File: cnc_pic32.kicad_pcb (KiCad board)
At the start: 4 copper layers, 96 x 96 mm, 111 parts, among them J1 icd, J13 mrf24j40_tp, J14 mrf24j40_tp, J18 USB_B_Mini, J2 ST7789 oled 128x64, J20 pololu, J21 pololu, J22 pololu, J23 conector oled ST1306 128x32, J24 pololu, J25 pololu, J5 USB_B_Mini, Q1 2N7002, SW2 up, U1 PIC32MX795F512L-80x-PF, U2 FT232BM, U3 LM1117DT-3.3, U4 MRF24J40MA, U5 LM1117DT-3.3, Y2 6MHZ

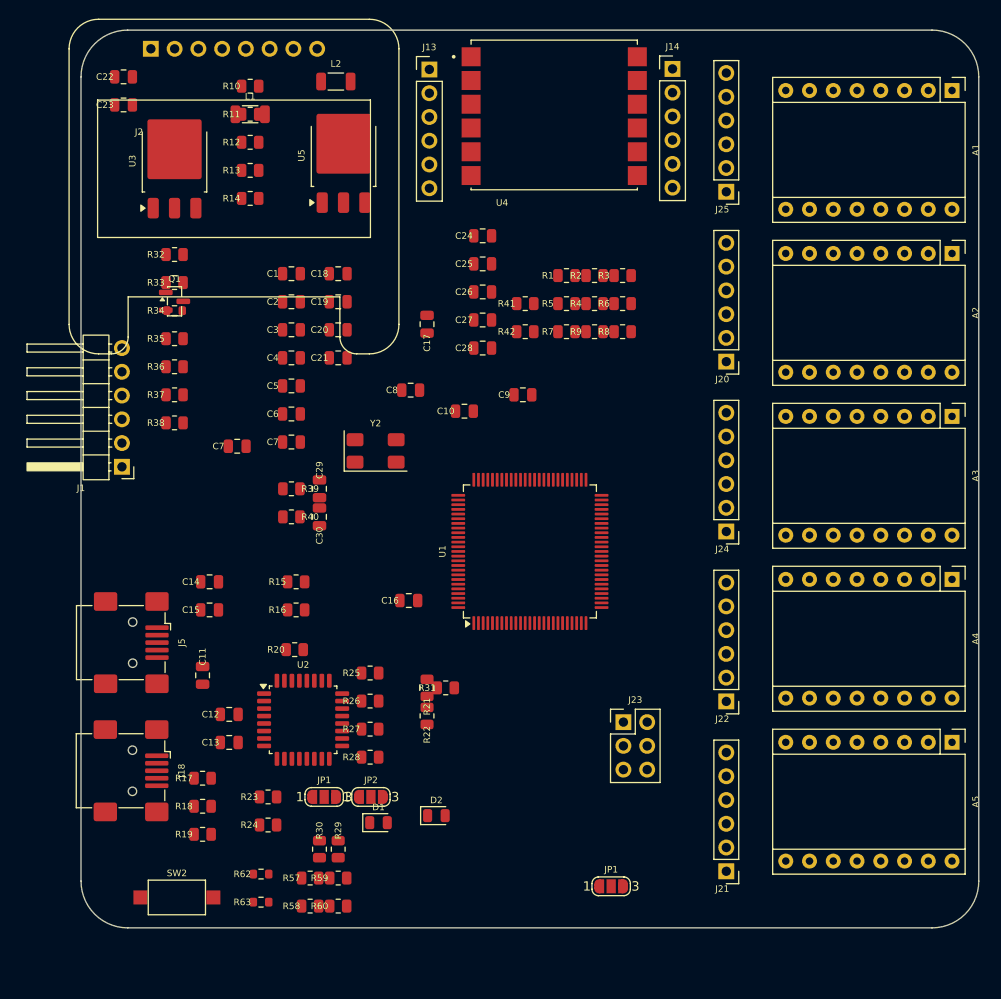
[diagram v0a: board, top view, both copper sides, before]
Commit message: feat: PCB layout updates, schematic changes, fp-lib-table config
- cnc_pic32.kicad_pcb: component repositioning, board outline, text formatting
- cnc_pic32.kicad_prl/pro: project settings updates
- fp-lib-table: add Library path to Library.pretty
- mcu.kicad_sch: PIC32 pin configuration updates
- zigbee.kicad_sch: MRF24J40 module updates
- oscilator.kicad_sch: crystal configuration
- power.kicad_sch/power_ft232.kicad_sch: power supply updates
- oled.kicad_sch: OLED display connections
- idc.kicad_sch: IDC connector updates
- osc_ft232.kicad_sch: FT232 crystal
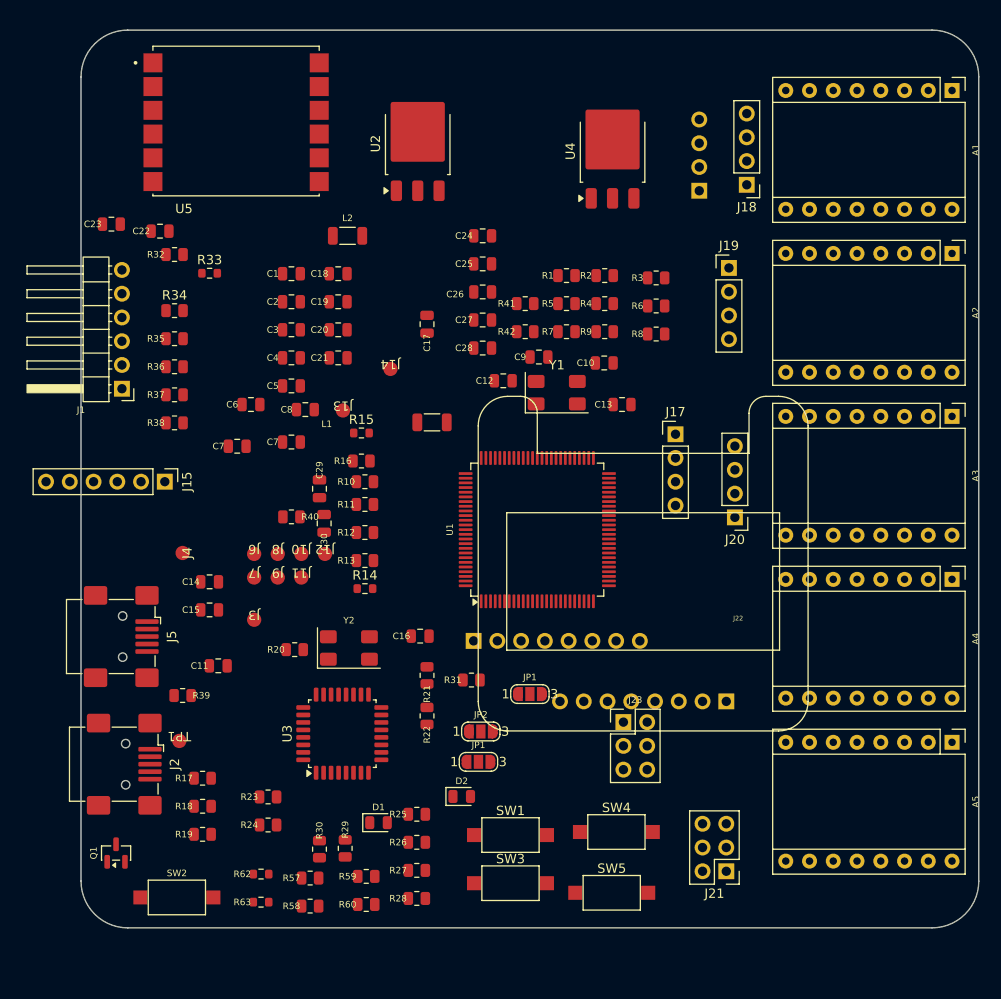
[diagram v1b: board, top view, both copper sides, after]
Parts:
- removed J25: pololu, kiC:PinHeader_1x06_P2.54mm_Vertical
- added J10: tp_ft232_, Library:connector_pin1, F.Cu at (75.6, 82.0)
- added J11: tp_ft232_, Library:connector_pin1, F.Cu at (75.6, 84.5)
- added J12: tp_ft232_, Library:connector_pin1, F.Cu at (78.1, 82.0)
- added J15: pololu, Library:PinHeader_1x06_P2.54mm_Vertical, F.Cu at (61.0, 74.3)
- added J16: pololu, Connector_PinHeader_2.54mm:PinHeader_1x04_P2.54mm_Vertical, B.Cu at (118.1, 43.2)
- added J17: pololu, Connector_PinHeader_2.54mm:PinHeader_1x04_P2.54mm_Vertical, F.Cu at (115.6, 69.2)
- added J19: pololu, Connector_PinHeader_2.54mm:PinHeader_1x04_P2.54mm_Vertical, F.Cu at (121.3, 51.4)
- added J3: tp_ft232_, Library:connector_pin1, F.Cu at (70.5, 89.1)
- added J4: tp_ft232_, Library:connector_pin1, F.Cu at (62.9, 81.9)
- added J6: tp_ft232_, Library:connector_pin1, F.Cu at (70.5, 82.0)
- added J7: tp_ft232_, Library:connector_pin1, F.Cu at (70.5, 84.5)
- added J8: tp_ft232_, Library:connector_pin1, F.Cu at (73.0, 82.0)
- added J9: tp_ft232_, Library:connector_pin1, F.Cu at (73.0, 84.5)
- added SW1: power, Button_Switch_SMD:SW_SPST_CK_RS282G05A3, F.Cu at (97.9, 112.1)
- added SW3: down, Button_Switch_SMD:SW_SPST_CK_RS282G05A3, F.Cu at (97.9, 117.2)
- added SW4: left, Button_Switch_SMD:SW_SPST_CK_RS282G05A3, F.Cu at (109.2, 111.8)
- added SW5: rigth, Button_Switch_SMD:SW_SPST_CK_RS282G05A3, F.Cu at (108.8, 118.2)
- added TP1: tp_pic+5, Library:connector_pin1, F.Cu at (62.5, 102.0)
- added Y1: 8MHZ, Crystal:Crystal_SMD_0603-4Pin_6.0x3.5mm, F.Cu at (102.9, 64.8)
- C10, C16, C9: value 15p -> 100nf
- C12, C13: value 33nf -> 15p
- C17: value 15p -> 33nf
- C18: value 100nf -> 33nf
- C21, C22: value 100nf -> 15p
- J13, J14: value mrf24j40_tp -> tp_ft232_; footprint Connector_PinHeader_2.54mm:PinHeader_1x06_P2.54mm_Vertical -> Library:connector_pin1
- J18: value USB_B_Mini -> pololu; footprint Connector_USB:USB_Mini-B_Wuerth_65100516121_Horizontal -> Connector_PinHeader_2.54mm:PinHeader_1x04_P2.54mm_Vertical
- J2: value ST7789 oled 128x64 -> USB_B_Mini; footprint kiC:Adafruit_SSD1306_No_Mounting_Holes_pads -> Library:USB_Mini-B_Wuerth_65100516121_Horizontal
- J20: footprint kiC:PinHeader_1x06_P2.54mm_Vertical -> Connector_PinHeader_2.54mm:PinHeader_1x04_P2.54mm_Vertical
- J21: value pololu -> conector oled ST1306 128x32; footprint kiC:PinHeader_1x06_P2.54mm_Vertical -> Connector_PinHeader_2.54mm:PinHeader_2x03_P2.54mm_Vertical
- J22: value pololu -> Adafruit ST7789; footprint kiC:PinHeader_1x06_P2.54mm_Vertical -> Library:Adafruit_SSD1306_No_Mounting_Holes_pads
- J24: value pololu -> Adafruit ST7789; footprint kiC:PinHeader_1x06_P2.54mm_Vertical -> Library:Adafruit_SSD1306_No_Mounting_Holes_pads; moved to B.Cu
- J5: footprint Connector_USB:USB_Mini-B_Wuerth_65100516121_Horizontal -> Library:USB_Mini-B_Wuerth_65100516121_Horizontal
- R1, R22: value 100 -> 10K
- R10, R13: value 10K -> 2k2
- R11, R12: value 0 -> 2k2
- R14: value 100 -> 2k2; footprint Resistor_SMD:R_0805_2012Metric -> Resistor_SMD:R_0603_1608Metric
- R15: value 1K -> 2k2; footprint Resistor_SMD:R_0805_2012Metric -> Resistor_SMD:R_0603_1608Metric
- R16: value 1M -> 10K
- R2: value 100 -> 0
- R20: value 10K -> 100
- R24: value 10K -> 1K5
- R27: value 1K5 -> 4K7
- R28: value 4K7 -> 27
- R3: value 10K -> 0
- R30: value 27 -> 10K
- R31: value 10K -> 1k
- R32, R38: value 2k2 -> 1k
- R33: footprint Resistor_SMD:R_0805_2012Metric -> Resistor_SMD:R_0603_1608Metric
- R34: footprint Resistor_SMD:R_0603_1608Metric -> Resistor_SMD:R_0805_2012Metric
- R39: value 22 -> 1k
- R4: value 22 -> 10K
- R5: value 1k -> 100
- R6: value 22 -> 1K
- R7: value 100 -> 1M
- R8: value 100 -> 22
- R9: value 1k -> 22
- U2: value FT232BM -> LM1117DT-3.3; footprint Package_QFP:LQFP-32_7x7mm_P0.8mm -> Package_TO_SOT_SMD:TO-252-3_TabPin2
- U3: value LM1117DT-3.3 -> FT232BM; footprint Package_TO_SOT_SMD:TO-252-3_TabPin2 -> Package_QFP:LQFP-32_7x7mm_P0.8mm
- U4: value MRF24J40MA -> LM1117DT-3.3; footprint Library:MODULE_MRF24J40MA -> Package_TO_SOT_SMD:TO-252-3_TabPin2
- U5: value LM1117DT-3.3 -> MRF24J40MA; footprint Package_TO_SOT_SMD:TO-252-3_TabPin2 -> Library:MODULE_MRF24J40MA
- moved J18 90.8 mm to (123.2, 42.5), turned to 180 degrees
- moved J2 76.5 mm to (56.8, 104.5), turned to -90 degrees
- moved U3 63.8 mm to (79.9, 101.2)
- moved U2 62.8 mm to (88.0, 38.1), turned to 90 degrees
- moved Q1 59.3 mm to (55.8, 114.0), turned to 90 degrees
- moved C13 55.4 mm to (109.9, 66.0)
- moved C12 46.2 mm to (97.2, 63.5)
- moved R10 44.0 mm to (82.4, 74.3)
- moved J14 44.0 mm to (85.1, 62.2)
- moved R11 43.5 mm to (82.4, 76.7)
- moved R12 43.5 mm to (82.4, 79.7)
- moved R13 43.5 mm to (82.4, 82.7)
- moved R14 43.5 mm to (82.4, 85.7)
- moved L1 38.3 mm to (89.5, 67.9)
- moved J13 37.6 mm to (80.0, 66.7)
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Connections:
- A1 pad 13: unconnected-(A1-~{RESET}-Pad13) -> /MCU/RA0
- A1 pad 14: unconnected-(A1-~{SLEEP}-Pad14) -> /MCU/RA1
- A1 pad 15: unconnected-(A1-STEP-Pad15) -> /MCU/RA3
- A1 pad 16: unconnected-(A1-DIR-Pad16) -> /MCU/RA4
- A1 pad 9: unconnected-(A1-~{ENABLE}-Pad9) -> /MCU/RA2
- A2 pad 13: unconnected-(A2-~{RESET}-Pad13) -> /MCU/RA5
- A2 pad 14: unconnected-(A2-~{SLEEP}-Pad14) -> /MCU/RA6
- A2 pad 15: unconnected-(A2-STEP-Pad15) -> /MCU/RA9
- A2 pad 16: unconnected-(A2-DIR-Pad16) -> /MCU/RA10
- A2 pad 9: unconnected-(A2-~{ENABLE}-Pad9) -> /MCU/RA7
- A3 pad 13: unconnected-(A3-~{RESET}-Pad13) -> /MCU/RB0
- A3 pad 14: unconnected-(A3-~{SLEEP}-Pad14) -> /MCU/RB1
- A3 pad 15: unconnected-(A3-STEP-Pad15) -> /MCU/RB3
- A3 pad 16: unconnected-(A3-DIR-Pad16) -> /MCU/RB4
- A3 pad 9: unconnected-(A3-~{ENABLE}-Pad9) -> /MCU/RB2
- A4 pad 13: unconnected-(A4-~{RESET}-Pad13) -> /MCU/RE9
- A4 pad 14: unconnected-(A4-~{SLEEP}-Pad14) -> /MCU/RE8
- A4 pad 15: unconnected-(A4-STEP-Pad15) -> /MCU/RE6
- A4 pad 9: unconnected-(A4-~{ENABLE}-Pad9) -> /MCU/RE7
- A5 pad 13: unconnected-(A5-~{RESET}-Pad13) -> /MCU/RE4
- A5 pad 14: unconnected-(A5-~{SLEEP}-Pad14) -> /MCU/RE3
- A5 pad 15: unconnected-(A5-STEP-Pad15) -> /MCU/RE1
- A5 pad 16: unconnected-(A5-DIR-Pad16) -> /MCU/RE0
- A5 pad 9: unconnected-(A5-~{ENABLE}-Pad9) -> /MCU/RE2
- C10 pad 1: /oscilator/OSC1 -> +3.3V
- C11 pad 1: /Ft232/mclr -> +3.3V
- C11 pad 2: /Ft232/FT_CTS -> GND
- C12 pad 1: Net-(U2-AVCC) -> Net-(C12-Pad1)
- C13 pad 1: Net-(J3-Pin_1) -> /MCU/OSC2
- C14 pad 2: /Ft232/V+_USB -> Net-(TP1-Pin_1)
- C16 pad 1: /Ft232/FT_XTIN -> /Ft232/mclr
- C16 pad 2: GND -> /Ft232/FT_CTS
- C17 pad 1: /Ft232/FT_XTOUT -> Net-(U3-AVCC)
- C18 pad 1: +3V3 -> Net-(J3-Pin_1)
- C19 pad 1: +3V3 -> GND
- C19 pad 2: GND -> /Ft232/V+_USB
- C21 pad 1: GND -> /Ft232/FT_XTIN
- C21 pad 2: +3V3 -> GND
- C22 pad 1: +3.3V -> /Ft232/FT_XTOUT
- C23 pad 1: +3.3V -> +3V3
- C24 pad 1: +3.3V -> +3V3
- C25 pad 1: +3.3V -> GND
- C25 pad 2: GND -> +3V3
- C26 pad 1: +3.3V -> GND
- C26 pad 2: GND -> +3V3
- C6 pad 1: unconnected-(C6-Pad1) -> +3.3V
- C6 pad 2: unconnected-(C6-Pad2) -> GND
- C7 pad 1: unconnected-(C7-Pad1) -> +3.3V
- C7 pad 2: unconnected-(C7-Pad2) -> GND
- C9 pad 1: Net-(C9-Pad1) -> +3.3V
- J13 pad 1: GND -> /Ft232/tp_ft232/FT_DTR
- J14 pad 1: GND -> /Ft232/tp_ft232/+5v
- J18 pad 1: Net-(J18-VBUS) -> Net-(A3-2B)
- J18 pad 2: Net-(J18-D-) -> Net-(A3-2A)
- J18 pad 3: Net-(J18-D+) -> Net-(A3-1A)
- J18 pad 4: unconnected-(J18-ID-Pad4) -> Net-(A3-1B)
- J2 pad 1: GND -> Net-(J2-VBUS)
- J2 pad 2: +3.3V -> Net-(J2-D-)
- J2 pad 3: /Oled/sda -> Net-(J2-D+)
- J2 pad 4: /Oled/scl -> unconnected-(J2-ID-Pad4)
- J2 pad 5: unconnected-(J2-Pin_5-Pad5) -> GND
- J2 pad 6: unconnected-(J2-Pin_6-Pad6) -> GND
- J20 pad 1: Net-(A2-2B) -> Net-(A5-2B)
- J20 pad 2: Net-(A2-2A) -> Net-(A5-2A)
- J20 pad 3: Net-(A2-1A) -> Net-(A5-1A)
- J20 pad 4: Net-(A2-1B) -> Net-(A5-1B)
- J21 pad 1: Net-(A5-2B) -> GND
- J21 pad 2: Net-(A5-2A) -> +3.3V
- J21 pad 3: Net-(A5-1A) -> /MCU/scl
- J21 pad 4: Net-(A5-1B) -> /MCU/sda
- J21 pad 5: (no net) -> unconnected-(J21-Pin_5-Pad5)
- J21 pad 6: (no net) -> unconnected-(J21-Pin_6-Pad6)
- J22 pad 1: Net-(A4-2B) -> GND
- J22 pad 2: Net-(A4-2A) -> +3.3V
- J22 pad 3: Net-(A4-1A) -> /MCU/sda
- J22 pad 4: Net-(A4-1B) -> /MCU/scl
- J22 pad 5: (no net) -> unconnected-(J22-Pin_5-Pad5)
- J22 pad 6: (no net) -> unconnected-(J22-Pin_6-Pad6)
- J23 pad 3: /Oled/scl -> /MCU/scl
- J23 pad 4: /Oled/sda -> /MCU/sda
- J24 pad 1: Net-(A3-2B) -> GND
- J24 pad 2: Net-(A3-2A) -> +3.3V
- J24 pad 3: Net-(A3-1A) -> /MCU/sda
- J24 pad 4: Net-(A3-1B) -> /MCU/scl
- J24 pad 5: (no net) -> unconnected-(J24-Pin_5-Pad5)
- J24 pad 6: (no net) -> unconnected-(J24-Pin_6-Pad6)
- JP1 pad 1: TXD -> RXD
- JP1 pad 2: /Ft232/TX_MCU -> /Ft232/RX_MCU
- JP1 pad 3: TX_Rpi -> RX_Rpi
- JP2 pad 1: RXD -> TXD
- JP2 pad 2: /Ft232/RX_MCU -> /Ft232/TX_MCU
- JP2 pad 3: RX_Rpi -> TX_Rpi
- L1 pad 1: Net-(J4-Pin_1) -> Net-(J2-VBUS)
- L1 pad 2: /Ft232/V+_USB -> Net-(TP1-Pin_1)
- L2 pad 1: Net-(J18-VBUS) -> Net-(J4-Pin_1)
- L2 pad 2: Net-(TP17-Pin_1) -> /Ft232/V+_USB
- R1 pad 1: unconnected-(R1-Pad1) -> +3.3V
- R1 pad 2: unconnected-(R1-Pad2) -> /Ft232/mclr
- R10 pad 2: /Ft232/mclr -> /MCU/RD5
- R11 pad 1: /MCU/RD0 -> +3.3V
- R11 pad 2: /MCU/scl -> /MCU/RD4
- R12 pad 1: /MCU/RD1 -> +12V
- R12 pad 2: /MCU/sda -> Net-(R12-Pad2)
- R13 pad 1: unconnected-(R13-Pad1) -> SW_PWR
- R13 pad 2: unconnected-(R13-Pad2) -> GND
- R14 pad 1: unconnected-(R14-Pad1) -> +3.3V
- R14 pad 2: unconnected-(R14-Pad2) -> /MCU/RD7
- R15 pad 1: /oscilator/OSC0 -> +3.3V
- R15 pad 2: Net-(C9-Pad1) -> /MCU/RD6
- R16 pad 1: Net-(C9-Pad1) -> Net-(Q1-D)
- R16 pad 2: /oscilator/OSC1 -> /Ft232/V+_USB
- R17 pad 1: Net-(Q1-D) -> GND
- R17 pad 2: /Ft232/V+_USB -> /Ft232/FT
- R18 pad 1: GND -> /Ft232/FT_PWR_EN
- R18 pad 2: /Ft232/FT -> Net-(Q1-G)
- R19 pad 1: /Ft232/FT_PWR_EN -> +3V3
- R19 pad 2: Net-(Q1-G) -> Net-(D1-A)
- R2 pad 1: unconnected-(R2-Pad1) -> /MCU/RD1
- R2 pad 2: unconnected-(R2-Pad2) -> /MCU/sda
- R20 pad 1: +3V3 -> Net-(U3-D0/TXD)
- R20 pad 2: Net-(D1-A) -> /Ft232/RX_MCU
- R21 pad 1: Net-(U2-D0/TXD) -> Net-(U3-D1/RXD)
- R21 pad 2: /Ft232/RX_MCU -> /Ft232/TX_MCU
- R22 pad 1: Net-(U2-D1/RXD) -> +3V3
- R22 pad 2: /Ft232/TX_MCU -> Net-(D2-A)
- R23 pad 2: Net-(D2-A) -> Net-(U3-~{SLEEP})
- R24 pad 1: +3V3 -> Net-(U3-AVCC)
- R24 pad 2: Net-(U2-~{SLEEP}) -> /Ft232/V+_USB
- R25 pad 1: Net-(U2-AVCC) -> /Ft232/FT_RST_OUT
- R25 pad 2: /Ft232/V+_USB -> /Ft232/FT_USB_DP
- R27 pad 1: /Ft232/FT_RST_OUT -> /Ft232/V+_USB
- R27 pad 2: /Ft232/FT_USB_DP -> /Ft232/FT_RESET
- R28 pad 1: /Ft232/V+_USB -> /Ft232/FT_USB_BM
- R28 pad 2: /Ft232/FT_RESET -> Net-(J5-D+)
- R29 pad 1: /Ft232/FT_USB_BM -> /Ft232/FT_USB_DP
- R29 pad 2: Net-(J5-D+) -> Net-(J5-D-)
- R3 pad 1: unconnected-(R3-Pad1) -> /MCU/RD0
- R3 pad 2: unconnected-(R3-Pad2) -> /MCU/scl
- R30 pad 1: /Ft232/FT_USB_DP -> +3V3
- R30 pad 2: Net-(J5-D-) -> /Ft232/FT_RESET
- R31 pad 1: +3V3 -> +3.3V
- R31 pad 2: /Ft232/power_ft232/FT_RESET -> /MCU/scl
- R32 pad 2: /zigbee/RESET_mrf -> /MCU/sda
- R33 pad 1: +3.3V -> /MCU/RA6
- R33 pad 2: /zigbee/int -> GND
- R34 pad 1: /zigbee/WAKE_mrf -> /MCU/RA2
- R34 pad 2: GND -> +3.3V
- R35 pad 1: /zigbee/MISO_spi4 -> /MCU/RA0
- R36 pad 1: /zigbee/CS_spi4 -> +3.3V
- R36 pad 2: +3.3V -> /MCU/RA5
- R37 pad 2: /zigbee/SCK_spi4 -> /MCU/RA3
- R38 pad 2: /zigbee/MOSI_spi4 -> /MCU/scl
- R39 pad 1: /Usb_pic32/D+ -> +3.3V
- R39 pad 2: Net-(J18-D+) -> /MCU/sda
- R40 pad 1: /Usb_pic32/D- -> /MCU/D-
- R40 pad 2: Net-(J18-D-) -> Net-(J4-D-)
- R41 pad 2: /Oled/sda -> /MCU/sda
- R42 pad 2: /Oled/scl -> /MCU/scl
- R6 pad 1: unconnected-(R6-Pad1) -> /MCU/OSC1
- R6 pad 2: unconnected-(R6-Pad2) -> Net-(C12-Pad1)
- R7 pad 1: unconnected-(R7-Pad1) -> Net-(C12-Pad1)
- R7 pad 2: unconnected-(R7-Pad2) -> /MCU/OSC2
- R8 pad 1: unconnected-(R8-Pad1) -> /MCU/D+
- R8 pad 2: unconnected-(R8-Pad2) -> Net-(J2-D+)
- R9 pad 1: unconnected-(R9-Pad1) -> /MCU/D-
- R9 pad 2: unconnected-(R9-Pad2) -> Net-(J2-D-)
- U1 pad 87: /MCU/RF0 -> /Ft232/RX_MCU
- U1 pad 88: /MCU/RF1 -> /Ft232/TX_MCU
- U2 pad 1: /Ft232/FT_EESK -> GND
- U2 pad 2: /Ft232/FT_EEDATA -> +3V3
- U2 pad 3: /Ft232/V+_USB -> Net-(TP1-Pin_1)
- U3 pad 1: GND -> /Ft232/FT_EESK
- U3 pad 2: +3V3 -> /Ft232/FT_EEDATA
- U4 pad 2: /zigbee/RESET_mrf -> +3V3
- U4 pad 3: /zigbee/WAKE_mrf -> /Ft232/V+_USB
- U5 pad 2: +3V3 -> /MCU/RA4
- U5 pad 3: Net-(TP17-Pin_1) -> /MCU/RA6

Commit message: fix: remove orphaned duplicate footprints C7 and JP1 from PCB
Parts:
- removed the C7 at (68.7, 70.5)
- removed the JP1 at (100.0, 97.0)
- moved J15 6.63 mm to (67.3, 76.2)
- moved J23 5.47 mm to (109.2, 105.4), turned to 90 degrees
- renumbered C18 to C31

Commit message: feat: PCB and project updates from KiCad
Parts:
- added C18: 33nf, Capacitor_SMD:C_0805_2012Metric, F.Cu at (99.5, 34.7)
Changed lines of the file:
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@@
 				)
 			)
-			(render_cache "C18" 0
+			(render_cache "C31" 0
 				(polygon
 					(pts
@@
 				(polygon
 					(pts
-						(xy 77.674047 52.3405) (xy 77.587964 52.3405) (xy 77.587964 51.790575) (xy 77.55371 51.819074)
-						(xy 77.506454 51.850029) (xy 77.456723 51.876938) (xy 77.41584 51.89461) (xy 77.41584 51.811176)
-						(xy 77.462669 51.786471) (xy 77.504614 51.75898) (xy 77.542059 51.728726) (xy 77.57641 51.694739)
-						(xy 77.601401 51.663542) (xy 77.618568 51.634735) (xy 77.674047 51.634735)
+						(xy 77.350316 52.154484) (xy 77.436399 52.143542) (xy 77.449783 52.19063) (xy 77.466811 52.224568)
+						(xy 77.486835 52.248261) (xy 77.512159 52.265984) (xy 77.54077 52.276641) (xy 77.573645 52.280318)
+						(xy 77.612359 52.275546) (xy 77.646127 52.261626) (xy 77.676184 52.238174) (xy 77.699388 52.207894)
+						(xy 77.713251 52.173505) (xy 77.718029 52.133711) (xy 77.713551 52.095716) (xy 77.70067 52.063505)
+						(xy 77.679305 52.035745) (xy 77.651445 52.014492) (xy 77.619066 52.001658) (xy 77.580826 51.997192)
+						(xy 77.555159 51.99932) (xy 77.520089 52.006766) (xy 77.52962 51.930172) (xy 77.543512 51.931155)
+						(xy 77.579336 51.927917) (xy 77.612115 51.918421) (xy 77.642503 51.902645) (xy 77.661596 51.886605)
+						(xy 77.675114 51.867123) (xy 77.683505 51.843522) (xy 77.686485 51.814681) (xy 77.682811 51.784673)
+						(xy 77.672187 51.759048) (xy 77.654429 51.736762) (xy 77.63144 51.719826) (xy 77.604267 51.709487)
+						(xy 77.571722 51.705859) (xy 77.539491 51.709499) (xy 77.511946 51.71998) (xy 77.488032 51.737317)
+						(xy 77.469271 51.760333) (xy 77.454749 51.79113) (xy 77.44499 51.831693) (xy 77.35895 51.81528)
+						(xy 77.369884 51.77313) (xy 77.385584 51.737459) (xy 77.405814 51.707317) (xy 77.430672 51.682009)
+						(xy 77.459831 51.661621) (xy 77.492308 51.646942) (xy 77.528715 51.637882) (xy 77.569841 51.634735)
+						(xy 77.607483 51.637528) (xy 77.642543 51.645738) (xy 77.675501 51.659312) (xy 77.70565 51.678045)
+						(xy 77.730055 51.70033) (xy 77.74936 51.726375) (xy 77.763684 51.75552) (xy 77.772138 51.785429)
+						(xy 77.774962 51.816562) (xy 77.772217 51.846067) (xy 77.764115 51.873419) (xy 77.750556 51.89914)
+						(xy 77.732249 51.921696) (xy 77.708473 51.941395) (xy 77.678364 51.958296) (xy 77.717553 51.971727)
+						(xy 77.749333 51.991585) (xy 77.77492 52.018007) (xy 77.793654 52.049813) (xy 77.805276 52.087147)
+						(xy 77.80937 52.13136) (xy 77.80511 52.176028) (xy 77.792663 52.216357) (xy 77.772006 52.253283)
+						(xy 77.742435 52.287456) (xy 77.707136 52.315207) (xy 77.667734 52.335029) (xy 77.623427 52.347212)
+						(xy 77.573132 52.351442) (xy 77.527643 52.347799) (xy 77.487517 52.337315) (xy 77.451825 52.320304)
+						(xy 77.419858 52.296603) (xy 77.392758 52.267291) (xy 77.372297 52.234266) (xy 77.358117 52.196943)
 					)
 				)
 				(polygon
 					(pts
-						(xy 78.168198 51.638352) (xy 78.207257 51.64865) (xy 78.241085 51.665175) (xy 78.270519 51.687993)
-						(xy 78.295256 51.716435) (xy 78.31252 51.747131) (xy 78.322914 51.780618) (xy 78.326469 51.817673)
-						(xy 78.323511 51.849334) (xy 78.314945 51.877358) (xy 78.300866 51.902474) (xy 78.281696 51.923934)
-						(xy 78.256212 51.942488) (xy 78.223203 51.958082) (xy 78.263914 51.975649) (xy 78.296242 51.998344)
-						(xy 78.321468 52.026214) (xy 78.339955 52.058998) (xy 78.351265 52.096064) (xy 78.355192 52.138456)
-						(xy 78.351105 52.18233) (xy 78.33921 52.221645) (xy 78.319567 52.257339) (xy 78.291591 52.290063)
-						(xy 78.258074 52.316418) (xy 78.219686 52.335454) (xy 78.175494 52.347291) (xy 78.124254 52.351442)
-						(xy 78.073007 52.347275) (xy 78.028806 52.335394) (xy 77.990406 52.31628) (xy 77.956874 52.289807)
-						(xy 77.928989 52.256997) (xy 77.909336 52.220944) (xy 77.89739 52.180958) (xy 77.893325 52.136618)
-						(xy 77.981708 52.136618) (xy 77.986018 52.172702) (xy 77.999147 52.207998) (xy 78.012693 52.229278)
-						(xy 78.029867 52.24698) (xy 78.051036 52.261426) (xy 78.086747 52.275584) (xy 78.125152 52.280318)
-						(xy 78.164631 52.275717) (xy 78.198127 52.262486) (xy 78.227007 52.240568) (xy 78.249183 52.211927)
-						(xy 78.262542 52.178705) (xy 78.267185 52.139524) (xy 78.262421 52.099744) (xy 78.248681 52.065884)
-						(xy 78.22581 52.036558) (xy 78.196138 52.014041) (xy 78.162075 52.00051) (xy 78.122288 51.995824)
-						(xy 78.083477 52.000457) (xy 78.050369 52.013826) (xy 78.021629 52.036087) (xy 77.999539 52.064978)
-						(xy 77.98629 52.098059) (xy 77.981708 52.136618) (xy 77.893325 52.136618) (xy 77.893274 52.136062)
-						(xy 77.897381 52.091475) (xy 77.909068 52.053615) (xy 77.927938 52.02117) (xy 77.95376 51.994044)
-						(xy 77.986247 51.973042) (xy 78.026673 51.958082) (xy 77.992711 51.942407) (xy 77.966694 51.923759)
-						(xy 77.9473 51.902218) (xy 77.933162 51.876897) (xy 77.924496 51.848189) (xy 77.921484 51.81528)
-						(xy 77.921756 51.812416) (xy 78.009448 51.812416) (xy 78.013169 51.844066) (xy 78.023834 51.87065)
-						(xy 78.041462 51.893327) (xy 78.064521 51.910519) (xy 78.091854 51.921015) (xy 78.124682 51.9247)
-						(xy 78.156574 51.921065) (xy 78.183378 51.910665) (xy 78.206234 51.893541) (xy 78.223949 51.87113)
-						(xy 78.234441 51.845992) (xy 78.238035 51.817203) (xy 78.234316 51.787176) (xy 78.223485 51.761103)
-						(xy 78.205251 51.738001) (xy 78.181766 51.720214) (xy 78.154938 51.709546) (xy 78.123741 51.705859)
-						(xy 78.092188 51.709491) (xy 78.065286 51.719948) (xy 78.041975 51.737275) (xy 78.023738 51.75984)
-						(xy 78.013066 51.784601) (xy 78.009448 51.812416) (xy 77.921756 51.812416) (xy 77.925003 51.778162)
-						(xy 77.935259 51.744868) (xy 77.952226 51.714598) (xy 77.976451 51.686796) (xy 78.005361 51.66455)
-						(xy 78.038773 51.64839) (xy 78.077543 51.638291) (xy 78.122801 51.634735)
+						(xy 78.218416 52.3405) (xy 78.132332 52.3405) (xy 78.132332 51.790575) (xy 78.098078 51.819074)
+						(xy 78.050822 51.850029) (xy 78.001091 51.876938) (xy 77.960208 51.89461) (xy 77.960208 51.811176)
+						(xy 78.007038 51.786471) (xy 78.048982 51.75898) (xy 78.086427 51.728726) (xy 78.120779 51.694739)
+						(xy 78.145769 51.663542) (xy 78.162936 51.634735) (xy 78.218416 51.634735)
 					)
 				)
@@
 			(offset
 				(xyz 0 0 0)
+			)
+			(scale
+				(xyz 1 1 1)
+			)
+			(rotate
+				(xyz 0 0 0)
+			)
+		)
+	)
+	(footprint "Capacitor_SMD:C_0805_2012Metric"
+		(layer "F.Cu")
+		(at 99.515 34.66)
+		(descr "Capacitor SMD 0805 (2012 Metric), square (rectangular) end terminal, IPC-7351 nominal, (Body size source: IPC-SM-782 page 76, https://www.pcb-3d.com/wordpress/wp-content/uploads/ipc-sm-782a_amendment_1_and_2.pdf, https://docs.google.com/spreadsheets/d/1BsfQQcO9C6DZCsRaXUlFlo91Tg2WpOkGARC1WS5S8t0/edit?usp=sharing)")
+		(tags "capacitor")
+		(property "Reference" "C18"
+			(at 0 -1.68 0)
+			(layer "F.SilkS")
+			(effects
+				(font
+					(size 1 1)
+					(thickness 0.15)
+				)
+			)
+		)
+		(property "Value" "33nf"
+			(at 0 1.68 0)
+			(layer "F.Fab")
+			(effects
+				(font
+					(size 1 1)
+					(thickness 0.15)
+				)
+			)
+		)
+		(property "Datasheet" ""
+			(at 0 0 0)
+			(layer "F.Fab")
+			(hide yes)
+			(effects
+				(font
+					(size 1.27 1.27)
+				)
+			)
+		)
+		(property "Description" ""
+			(at 0 0 0)
+			(layer "F.Fab")
+			(hide yes)
+			(effects
+				(font
+					(size 1.27 1.27)
+				)
+			)
+		)
+		(property ki_fp_filters "C_*")
+		(sheetname "/Ft232/")
+		(sheetfile "ft232.kicad_sch")
+		(units
+			(unit
+				(name "A")
+				(pins "1" "2")
+			)
+		)
+		(attr smd)
+		(duplicate_pad_numbers_are_jumpers no)
+		(fp_line
+			(start -0.261252 -0.735)
+			(end 0.261252 -0.735)
+			(stroke
+				(width 0.12)
+				(type solid)
+			)
+			(layer "F.SilkS")
+		)
+		(fp_line
+			(start -0.261252 0.735)
+			(end 0.261252 0.735)
+			(stroke
+				(width 0.12)
+				(type solid)
+			)
+			(layer "F.SilkS")
+		)
+		(fp_rect
+			(start -1.7 -0.98)
+			(end 1.7 0.98)
+			(stroke
+				(width 0.05)
+				(type solid)
+			)
+			(fill no)
+			(layer "F.CrtYd")
+		)
+		(fp_rect
+			(start -1 -0.625)
+			(end 1 0.625)
+			(stroke
+				(width 0.1)
+				(type solid)
+			)
+			(fill no)
+			(layer "F.Fab")
+		)
+		(fp_text user "${REFERENCE}"
+			(at 0 0 0)
+			(layer "F.Fab")
+			(effects
+				(font
+					(size 0.5 0.5)
+					(thickness 0.08)
+				)
+			)
+		)
+		(pad "1" smd roundrect
+			(at -0.95 0)
+			(size 1 1.45)
+			(layers "F.Cu" "F.Mask" "F.Paste")
+			(roundrect_rratio 0.25)
+			(net "Net-(J3-Pin_1)")
+			(pintype "passive")
+		)
+		(pad "2" smd roundrect
+			(at 0.95 0)
+			(size 1 1.45)
+			(layers "F.Cu" "F.Mask" "F.Paste")
+			(roundrect_rratio 0.25)
+			(net "GND")
+			(pintype "passive")
+		)
+		(embedded_fonts no)
+		(model "${KICAD10_3DMODEL_DIR}/Capacitor_SMD.3dshapes/C_0805_2012Metric.step"
+			(offset
+				(xyz 0 0 0)
